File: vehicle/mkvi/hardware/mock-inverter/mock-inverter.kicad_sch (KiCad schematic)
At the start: 64 parts, among them J1 MicroFit_RA_4, J2 TagConnect_6, J3 MicroFit_RA_3, K1 3350-4275, U1 MAX7221CWG_1, U2 ATMEGA16M1, U3 TLV76780DBVR, U4 MCP2561-E_SN, U5 ADUM4150ARIZ-RL, U6 ADS7816U, Y1 Crystal_SMD

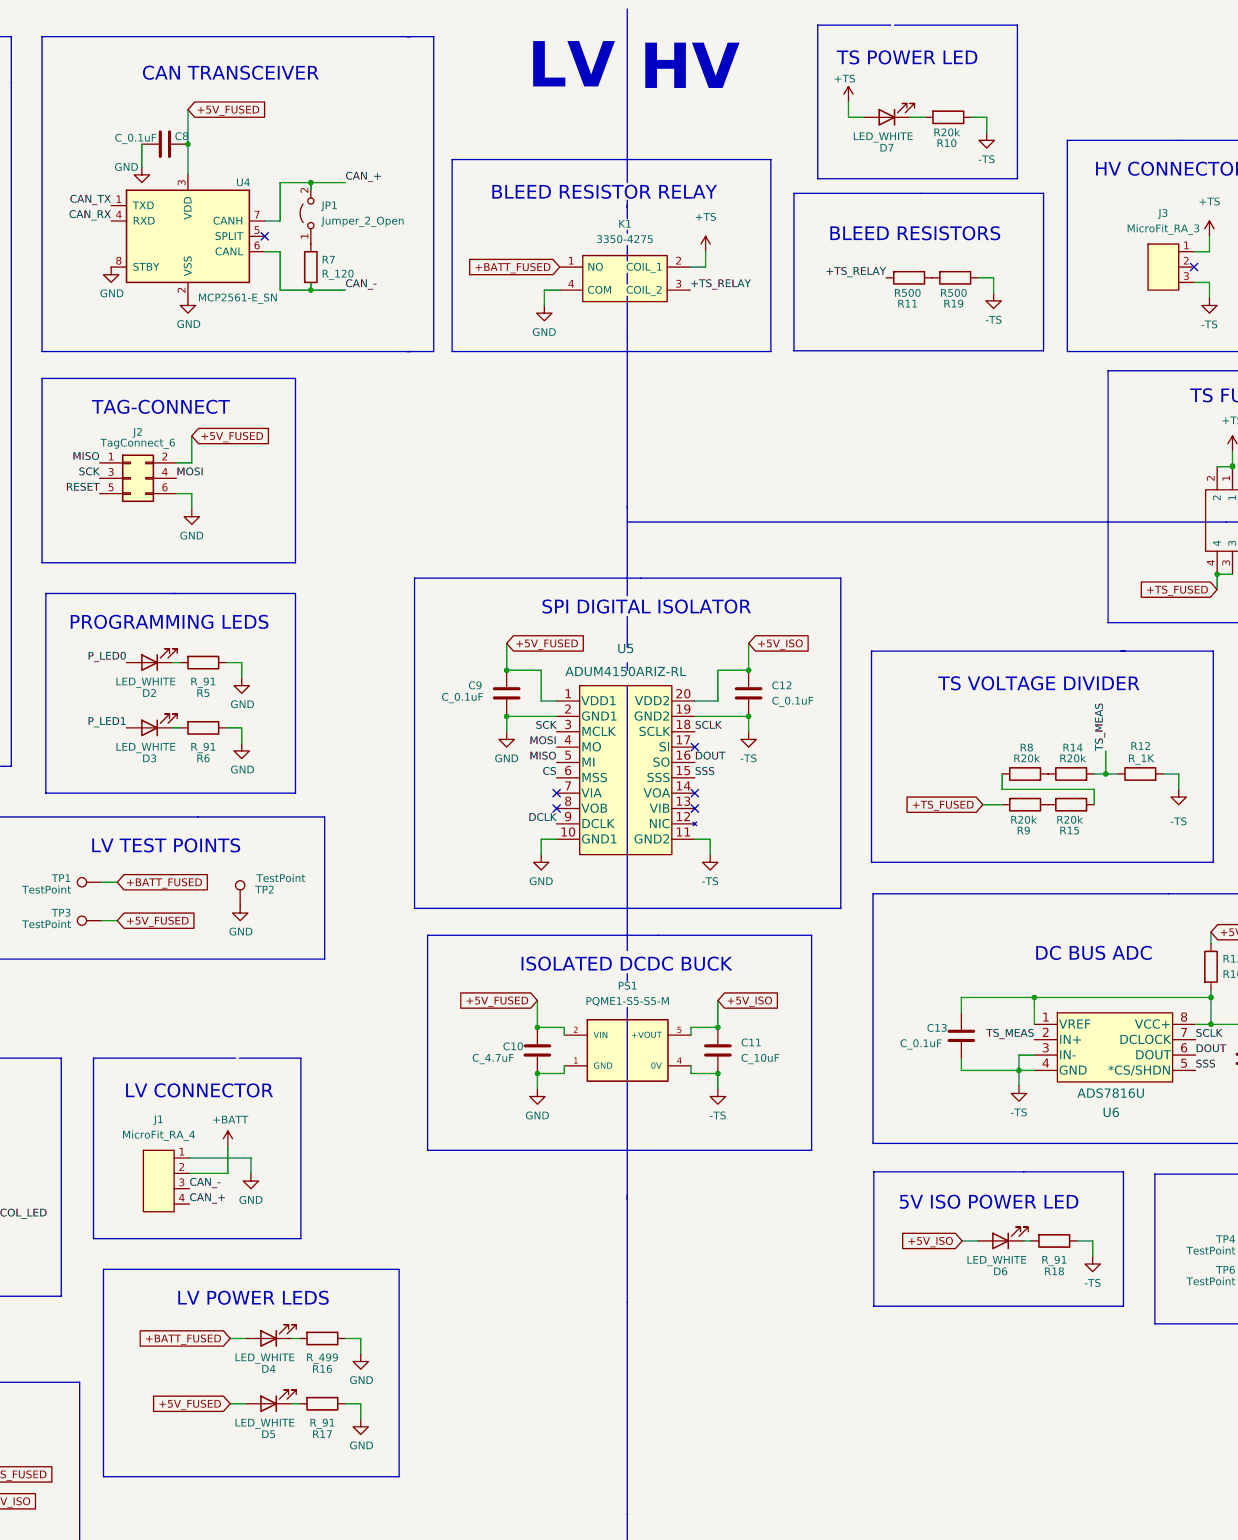
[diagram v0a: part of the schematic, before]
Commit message: Fix library associations for LEDs in schematic
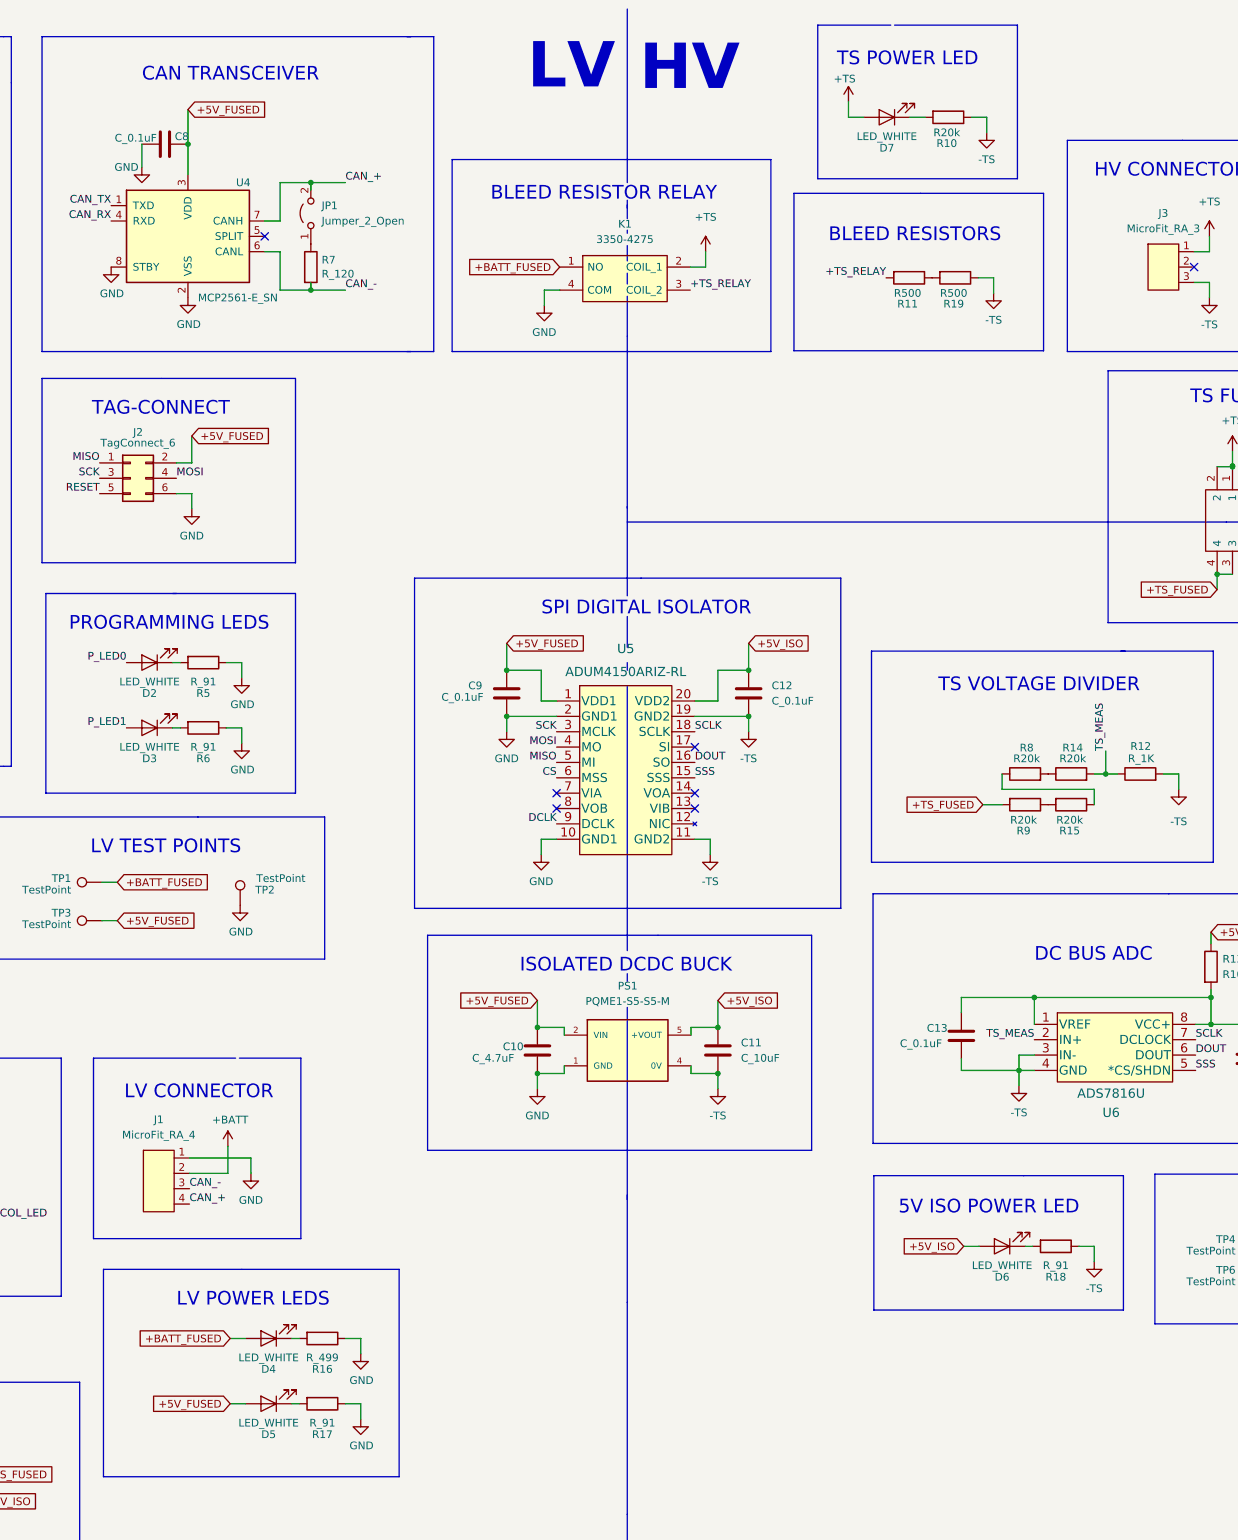
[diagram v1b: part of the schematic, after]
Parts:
- removed D2, D3, D4, D5, D6, D7: LED_WHITE, footprints:LED_0805_OEM, symbol OEM:LED_WHITE
- added D2, D3, D4, D5, D6, D7: LED_WHITE, footprints:LED_0805_OEM, symbol formula:LED_0805
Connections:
- net +5V: now also D7.2 (A)
- net +5V_FUSED: now also D5.2 (A)
- net +5V_ISO: now also D6.2 (A)
- net +BATT_FUSED: now also D4.2 (A)
- net P_LED0: now also D2.2 (A)
- net P_LED1: now also D3.2 (A)
- net at R6.2: now also D3.1 (K)
- net at R10.2: now also D7.1 (K)
- net at R17.2: now also D5.1 (K)
- net at R16.2: now also D4.1 (K)
- net at R5.2: now also D2.1 (K)
- net at R18.2: now also D6.1 (K)
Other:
- moved on the sheet: R18
